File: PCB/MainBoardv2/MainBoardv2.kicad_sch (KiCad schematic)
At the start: 63 parts, among them J1 Conn_02x03_Odd_Even, J2 USB_B_Micro, J3 Conn_02x03_Odd_Even, J4 Conn_01x05_Pin, J5 Screw_Terminal_01x02, J6 Conn_01x04_Socket, J7 Screw_Terminal_01x02, J8 Conn_01x04_Socket, J9 Conn_01x04_Socket, SW1 SW_Push, SW2 Toggle, U1 AZ1117-3.3, U2 STM32F103C8T6TR, U3 TPS56637RPA, Y1 8MHz Crystal

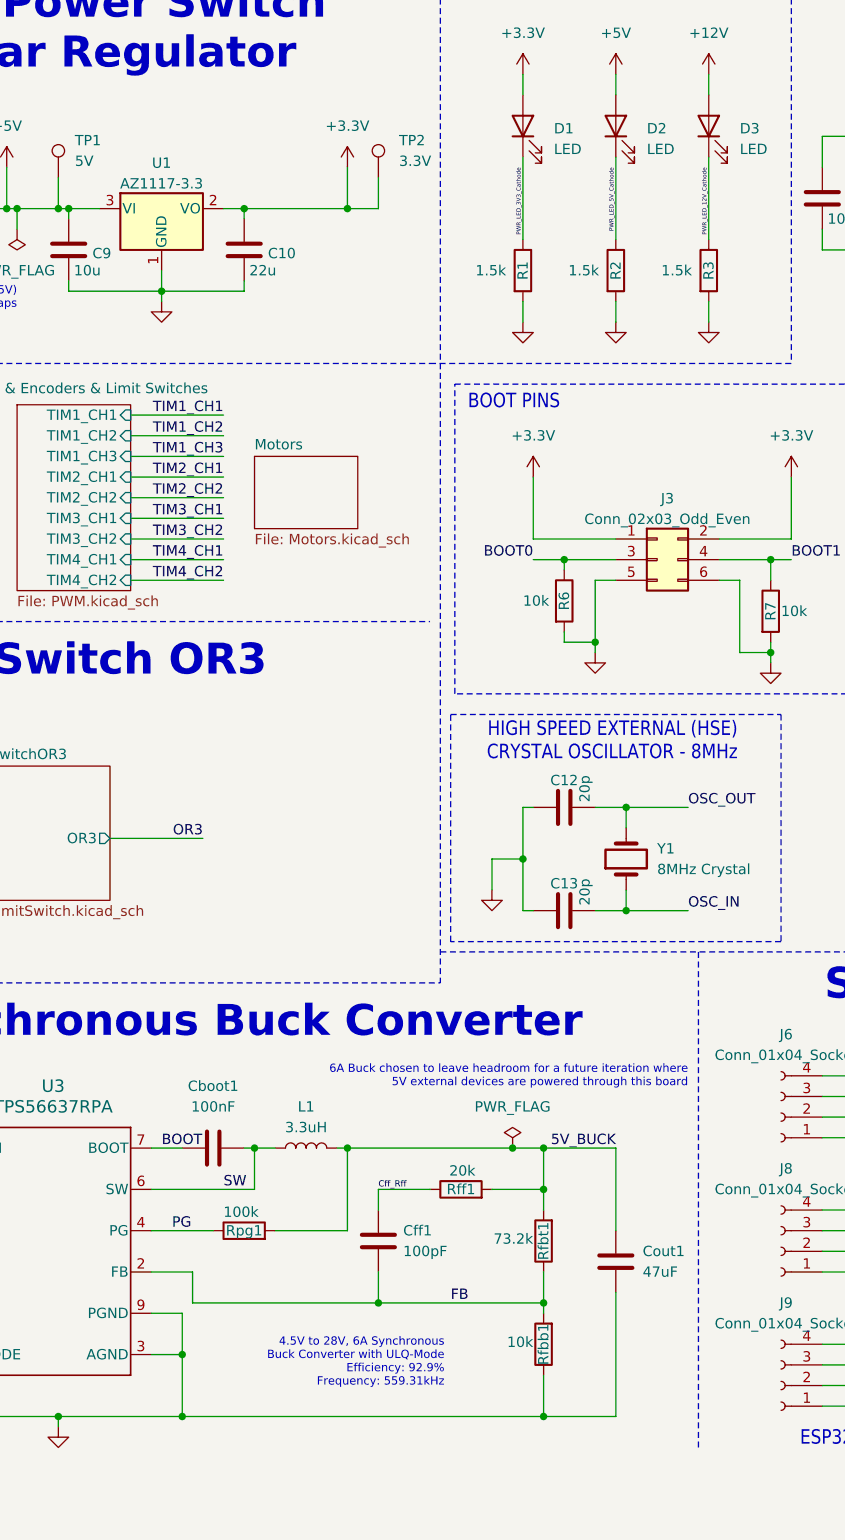
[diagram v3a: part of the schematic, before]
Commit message: PCB laid out & passes DRC
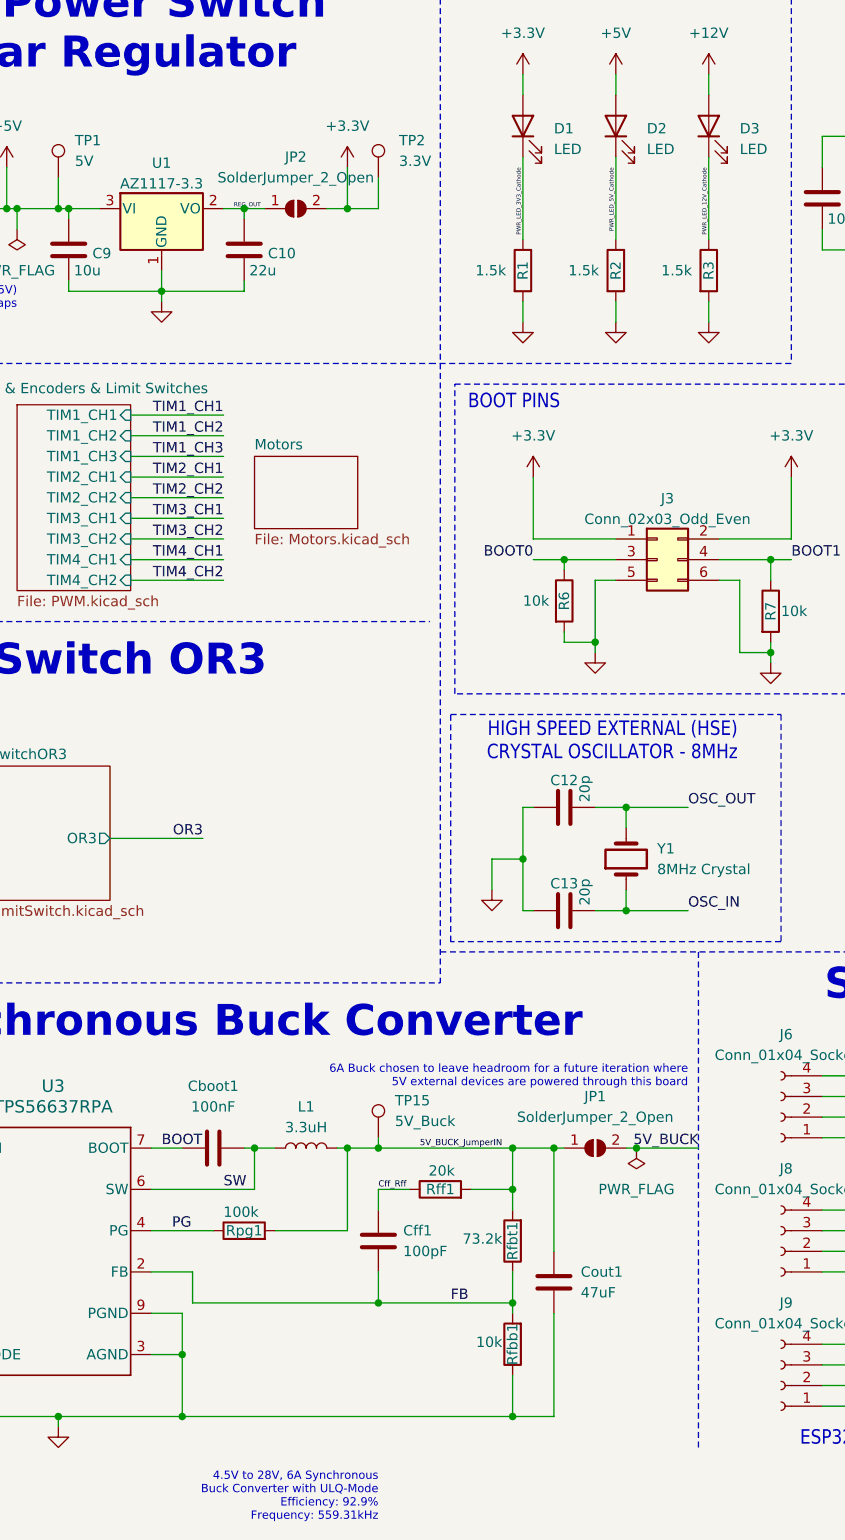
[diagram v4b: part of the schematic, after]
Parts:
- added JP1, JP2: SolderJumper_2_Open, Jumper:SolderJumper-2_P1.3mm_Open_TrianglePad1.0x1.5mm, symbol Jumper:SolderJumper_2_Open
- added TP15: 5V_Buck, TestPoint:TestPoint_Keystone_5000-5004_Miniature, symbol Connector:TestPoint
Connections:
- net +3.3V: now also JP2.2 (B); no longer C10.1, U1.2 (VO)
- net 5V_BUCK: now also JP1.2 (B); no longer Cout1.1, L1.2, Rfbt1.2, Rff1.2, Rpg1.2
- new net 5V_BUCK_JumperIN: Cout1.1, JP1.1 (A), L1.2, Rfbt1.2, Rff1.2, Rpg1.2, TP15.1
- new net REG_OUT: C10.1, JP2.1 (A), U1.2 (VO)
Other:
- moved on the sheet: Cout1, Rfbb1, Rfbt1, Rff1
